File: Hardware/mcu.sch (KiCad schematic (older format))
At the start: 10 parts, among them SW3 SW_PUSH, U1 STM32F411RE_LQFP64

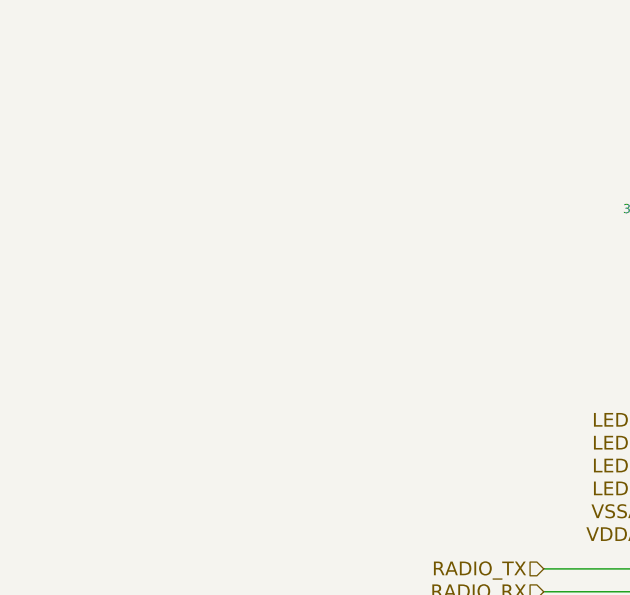
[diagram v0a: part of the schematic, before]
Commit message: Switched to tantalum capacitor for power supply
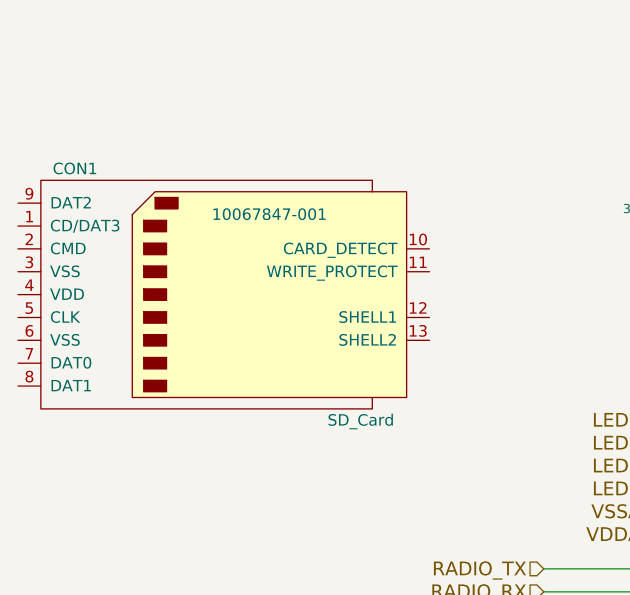
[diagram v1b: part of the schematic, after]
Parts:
- added CON1: SD_Card, 10067847-001, symbol SD_Card
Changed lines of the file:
@@
 LIBS:STM32-Additional
 LIBS:xbee
+LIBS:Passives
 LIBS:avbay-cache
 EELAYER 25 0
@@
 $EndDescr
 $Comp
-L 3V3 #PWR026
+L 3V3 #PWR24
 U 1 1 542CDA8F
 P 3800 3600
-F 0 "#PWR026" H 3800 3700 40  0001 C CNN
+F 0 "#PWR24" H 3800 3700 40  0001 C CNN
 F 1 "3V3" H 3800 3725 40  0000 C CNN
 F 2 "" H 3800 3600 60  0000 C CNN
@@
 $EndComp
 $Comp
-L GND #PWR027
+L GND #PWR26
 U 1 1 542CDA9E
 P 3850 3850
-F 0 "#PWR027" H 3850 3850 30  0001 C CNN
+F 0 "#PWR26" H 3850 3850 30  0001 C CNN
 F 1 "GND" H 3850 3780 30  0001 C CNN
 F 2 "" H 3850 3850 60  0000 C CNN
@@
 $EndComp
 $Comp
-L 3V3 #PWR028
+L 3V3 #PWR25
 U 1 1 542CDAB1
 P 3800 4800
-F 0 "#PWR028" H 3800 4900 40  0001 C CNN
+F 0 "#PWR25" H 3800 4900 40  0001 C CNN
 F 1 "3V3" H 3800 4925 40  0000 C CNN
 F 2 "" H 3800 4800 60  0000 C CNN
@@
 $EndComp
 $Comp
-L 3V3 #PWR029
+L 3V3 #PWR34
 U 1 1 542CDAB7
 P 7450 4850
-F 0 "#PWR029" H 7450 4950 40  0001 C CNN
+F 0 "#PWR34" H 7450 4950 40  0001 C CNN
 F 1 "3V3" H 7450 4975 40  0000 C CNN
 F 2 "" H 7450 4850 60  0000 C CNN
@@
 $EndComp
 $Comp
-L 3V3 #PWR030
+L 3V3 #PWR35
 U 1 1 542CDC4D
 P 7500 3350
-F 0 "#PWR030" H 7500 3450 40  0001 C CNN
+F 0 "#PWR35" H 7500 3450 40  0001 C CNN
 F 1 "3V3" H 7500 3475 40  0000 C CNN
 F 2 "" H 7500 3350 60  0000 C CNN
@@
 $EndComp
 $Comp
-L GND #PWR031
+L GND #PWR31
 U 1 1 5430D873
 P 6150 1450
-F 0 "#PWR031" H 6150 1450 30  0001 C CNN
+F 0 "#PWR31" H 6150 1450 30  0001 C CNN
 F 1 "GND" H 6150 1380 30  0001 C CNN
 F 2 "" H 6150 1450 60  0000 C CNN
@@
 $EndComp
 $Comp
-L 3V3 #PWR032
+L 3V3 #PWR36
 U 1 1 5430DC01
 P 7600 4350
-F 0 "#PWR032" H 7600 4450 40  0001 C CNN
+F 0 "#PWR36" H 7600 4450 40  0001 C CNN
 F 1 "3V3" H 7600 4475 40  0000 C CNN
 F 2 "" H 7600 4350 60  0000 C CNN
@@
 $EndComp
 $Comp
-L GND #PWR033
+L GND #PWR37
 U 1 1 5430DC07
 P 9000 4500
-F 0 "#PWR033" H 9000 4500 30  0001 C CNN
+F 0 "#PWR37" H 9000 4500 30  0001 C CNN
 F 1 "GND" H 9000 4430 30  0001 C CNN
 F 2 "" H 9000 4500 60  0000 C CNN
@@
 $EndComp
 $Comp
-L 3V3 #PWR034
+L 3V3 #PWR29
 U 1 1 5430E0CC
 P 5300 5450
-F 0 "#PWR034" H 5300 5550 40  0001 C CNN
+F 0 "#PWR29" H 5300 5550 40  0001 C CNN
 F 1 "3V3" H 5300 5575 40  0000 C CNN
 F 2 "" H 5300 5450 60  0000 C CNN
@@
 $EndComp
 $Comp
-L GND #PWR035
+L GND #PWR30
 U 1 1 5430E365
 P 5300 6050
-F 0 "#PWR035" H 5300 6050 30  0001 C CNN
+F 0 "#PWR30" H 5300 6050 30  0001 C CNN
 F 1 "GND" H 5300 5980 30  0001 C CNN
 F 2 "" H 5300 6050 60  0000 C CNN
@@
 $EndComp
 $Comp
-L GND #PWR036
+L GND #PWR23
 U 1 1 5430E5BA
 P 3550 4650
-F 0 "#PWR036" H 3550 4650 30  0001 C CNN
+F 0 "#PWR23" H 3550 4650 30  0001 C CNN
 F 1 "GND" H 3550 4580 30  0001 C CNN
 F 2 "" H 3550 4650 60  0000 C CNN
@@
 USART_RX
 $Comp
-L 3V3 #PWR037
+L 3V3 #PWR27
 U 1 1 5430E17B
 P 4050 1800
-F 0 "#PWR037" H 4050 1900 40  0001 C CNN
+F 0 "#PWR27" H 4050 1900 40  0001 C CNN
 F 1 "3V3" H 4050 1925 40  0000 C CNN
 F 2 "" H 4050 1800 60  0000 C CNN
@@
 	4150 4900 4150 5300
 $Comp
-L GND #PWR038
+L GND #PWR28
 U 1 1 54449600
 P 4150 5300
-F 0 "#PWR038" H 4150 5300 30  0001 C CNN
+F 0 "#PWR28" H 4150 5300 30  0001 C CNN
 F 1 "GND" H 4150 5230 30  0001 C CNN
 F 2 "" H 4150 5300 60  0000 C CNN
@@
 	7350 4900 7350 5100
 $Comp
-L GND #PWR039
+L GND #PWR32
 U 1 1 5444A762
 P 7350 3600
-F 0 "#PWR039" H 7350 3600 30  0001 C CNN
+F 0 "#PWR32" H 7350 3600 30  0001 C CNN
 F 1 "GND" H 7350 3530 30  0001 C CNN
 F 2 "" H 7350 3600 60  0000 C CNN
@@
 	7350 3300 7350 3600
 $Comp
-L GND #PWR040
+L GND #PWR33
 U 1 1 54449656
 P 7350 5100
-F 0 "#PWR040" H 7350 5100 30  0001 C CNN
+F 0 "#PWR33" H 7350 5100 30  0001 C CNN
 F 1 "GND" H 7350 5030 30  0001 C CNN
 F 2 "" H 7350 5100 60  0000 C CNN
@@
 Text HLabel 4150 3000 0    60   Input ~ 0
 VSSA
+$Comp
+L SD_Card CON1
+U 1 1 558E5943
+P 2250 2050
+F 0 "CON1" H 1600 2600 50  0000 C CNN
+F 1 "SD_Card" H 2850 1500 50  0000 C CNN
+F 2 "10067847-001" H 2450 2400 50  0000 C CNN
+F 3 "" H 2250 2050 60  0000 C CNN
+	1    2250 2050
+	1    0    0    -1
+$EndComp
 $EndSCHEMATC

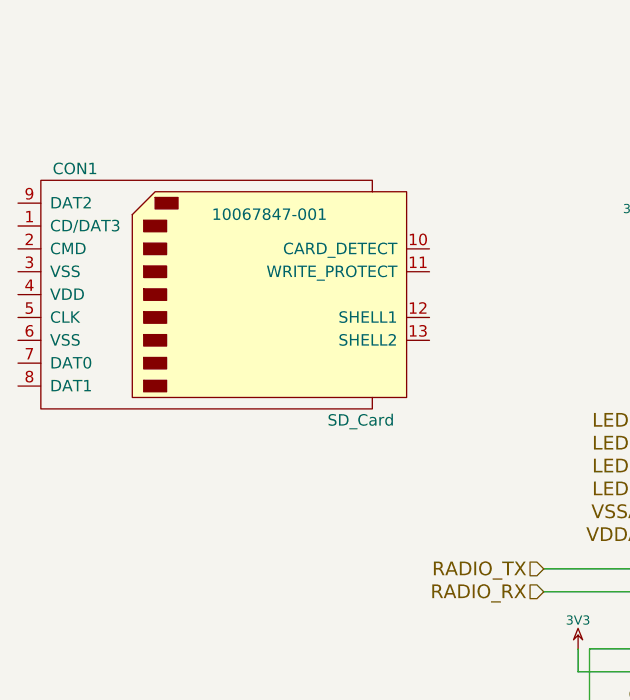
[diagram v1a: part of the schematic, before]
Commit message: Added MicroSD card
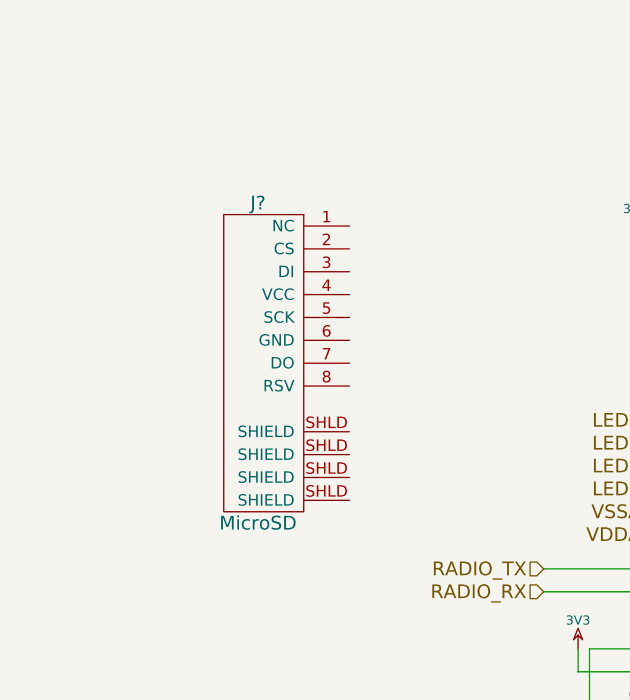
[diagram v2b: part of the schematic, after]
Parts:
- removed CON1: SD_Card, 10067847-001, symbol SD_Card
- added J?: MicroSD, symbol MicroSD
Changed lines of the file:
@@
 LIBS:xbee
 LIBS:Passives
+LIBS:DataStorage
 LIBS:avbay-cache
 EELAYER 25 0
@@
 $EndDescr
 $Comp
-L 3V3 #PWR24
+L 3V3 #PWR026
 U 1 1 542CDA8F
 P 3800 3600
-F 0 "#PWR24" H 3800 3700 40  0001 C CNN
+F 0 "#PWR026" H 3800 3700 40  0001 C CNN
 F 1 "3V3" H 3800 3725 40  0000 C CNN
 F 2 "" H 3800 3600 60  0000 C CNN
@@
 $EndComp
 $Comp
-L GND #PWR26
+L GND #PWR027
 U 1 1 542CDA9E
 P 3850 3850
-F 0 "#PWR26" H 3850 3850 30  0001 C CNN
+F 0 "#PWR027" H 3850 3850 30  0001 C CNN
 F 1 "GND" H 3850 3780 30  0001 C CNN
 F 2 "" H 3850 3850 60  0000 C CNN
@@
 $EndComp
 $Comp
-L 3V3 #PWR25
+L 3V3 #PWR028
 U 1 1 542CDAB1
 P 3800 4800
-F 0 "#PWR25" H 3800 4900 40  0001 C CNN
+F 0 "#PWR028" H 3800 4900 40  0001 C CNN
 F 1 "3V3" H 3800 4925 40  0000 C CNN
 F 2 "" H 3800 4800 60  0000 C CNN
@@
 $EndComp
 $Comp
-L 3V3 #PWR34
+L 3V3 #PWR029
 U 1 1 542CDAB7
 P 7450 4850
-F 0 "#PWR34" H 7450 4950 40  0001 C CNN
+F 0 "#PWR029" H 7450 4950 40  0001 C CNN
 F 1 "3V3" H 7450 4975 40  0000 C CNN
 F 2 "" H 7450 4850 60  0000 C CNN
@@
 $EndComp
 $Comp
-L 3V3 #PWR35
+L 3V3 #PWR030
 U 1 1 542CDC4D
 P 7500 3350
-F 0 "#PWR35" H 7500 3450 40  0001 C CNN
+F 0 "#PWR030" H 7500 3450 40  0001 C CNN
 F 1 "3V3" H 7500 3475 40  0000 C CNN
 F 2 "" H 7500 3350 60  0000 C CNN
@@
 $EndComp
 $Comp
-L GND #PWR31
+L GND #PWR031
 U 1 1 5430D873
 P 6150 1450
-F 0 "#PWR31" H 6150 1450 30  0001 C CNN
+F 0 "#PWR031" H 6150 1450 30  0001 C CNN
 F 1 "GND" H 6150 1380 30  0001 C CNN
 F 2 "" H 6150 1450 60  0000 C CNN
@@
 $EndComp
 $Comp
-L 3V3 #PWR36
+L 3V3 #PWR032
 U 1 1 5430DC01
 P 7600 4350
-F 0 "#PWR36" H 7600 4450 40  0001 C CNN
+F 0 "#PWR032" H 7600 4450 40  0001 C CNN
 F 1 "3V3" H 7600 4475 40  0000 C CNN
 F 2 "" H 7600 4350 60  0000 C CNN
@@
 $EndComp
 $Comp
-L GND #PWR37
+L GND #PWR033
 U 1 1 5430DC07
 P 9000 4500
-F 0 "#PWR37" H 9000 4500 30  0001 C CNN
+F 0 "#PWR033" H 9000 4500 30  0001 C CNN
 F 1 "GND" H 9000 4430 30  0001 C CNN
 F 2 "" H 9000 4500 60  0000 C CNN
@@
 $EndComp
 $Comp
-L 3V3 #PWR29
+L 3V3 #PWR034
 U 1 1 5430E0CC
 P 5300 5450
-F 0 "#PWR29" H 5300 5550 40  0001 C CNN
+F 0 "#PWR034" H 5300 5550 40  0001 C CNN
 F 1 "3V3" H 5300 5575 40  0000 C CNN
 F 2 "" H 5300 5450 60  0000 C CNN
@@
 $EndComp
 $Comp
-L GND #PWR30
+L GND #PWR035
 U 1 1 5430E365
 P 5300 6050
-F 0 "#PWR30" H 5300 6050 30  0001 C CNN
+F 0 "#PWR035" H 5300 6050 30  0001 C CNN
 F 1 "GND" H 5300 5980 30  0001 C CNN
 F 2 "" H 5300 6050 60  0000 C CNN
@@
 $EndComp
 $Comp
-L GND #PWR23
+L GND #PWR036
 U 1 1 5430E5BA
 P 3550 4650
-F 0 "#PWR23" H 3550 4650 30  0001 C CNN
+F 0 "#PWR036" H 3550 4650 30  0001 C CNN
 F 1 "GND" H 3550 4580 30  0001 C CNN
 F 2 "" H 3550 4650 60  0000 C CNN
@@
 USART_RX
 $Comp
-L 3V3 #PWR27
+L 3V3 #PWR037
 U 1 1 5430E17B
 P 4050 1800
-F 0 "#PWR27" H 4050 1900 40  0001 C CNN
+F 0 "#PWR037" H 4050 1900 40  0001 C CNN
 F 1 "3V3" H 4050 1925 40  0000 C CNN
 F 2 "" H 4050 1800 60  0000 C CNN
@@
 	4150 4900 4150 5300
 $Comp
-L GND #PWR28
+L GND #PWR038
 U 1 1 54449600
 P 4150 5300
-F 0 "#PWR28" H 4150 5300 30  0001 C CNN
+F 0 "#PWR038" H 4150 5300 30  0001 C CNN
 F 1 "GND" H 4150 5230 30  0001 C CNN
 F 2 "" H 4150 5300 60  0000 C CNN
@@
 	7350 4900 7350 5100
 $Comp
-L GND #PWR32
+L GND #PWR039
 U 1 1 5444A762
 P 7350 3600
-F 0 "#PWR32" H 7350 3600 30  0001 C CNN
+F 0 "#PWR039" H 7350 3600 30  0001 C CNN
 F 1 "GND" H 7350 3530 30  0001 C CNN
 F 2 "" H 7350 3600 60  0000 C CNN
@@
 	7350 3300 7350 3600
 $Comp
-L GND #PWR33
+L GND #PWR040
 U 1 1 54449656
 P 7350 5100
-F 0 "#PWR33" H 7350 5100 30  0001 C CNN
+F 0 "#PWR040" H 7350 5100 30  0001 C CNN
 F 1 "GND" H 7350 5030 30  0001 C CNN
 F 2 "" H 7350 5100 60  0000 C CNN
@@
 VSSA
 $Comp
-L SD_Card CON1
-U 1 1 558E5943
-P 2250 2050
-F 0 "CON1" H 1600 2600 50  0000 C CNN
-F 1 "SD_Card" H 2850 1500 50  0000 C CNN
-F 2 "10067847-001" H 2450 2400 50  0000 C CNN
-F 3 "" H 2250 2050 60  0000 C CNN
-	1    2250 2050
-	1    0    0    -1
-$EndComp
+L MicroSD J?
+U 1 1 558E636D
+P 2600 2350
+F 0 "J?" H 2400 3050 60  0000 C CNN
+F 1 "MicroSD" H 2400 1650 60  0000 C CNN
+F 2 "" H 2700 2500 60  0000 C CNN
+F 3 "" H 2700 2500 60  0000 C CNN
+	1    2600 2350
+	1    0    0    -1
+$EndComp
